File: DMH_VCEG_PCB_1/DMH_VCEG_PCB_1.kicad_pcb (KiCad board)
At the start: 2 copper layers, 148 x 175 mm, 229 parts, among them J1 TS_Jack_6.35mm_Sw, J10 TS_Jack_6.35mm_Sw, J100 IDC_02x08, J11 TS_Jack_6.35mm_Sw, J12 TS_Jack_6.35mm_Sw, J13 TS_Jack_6.35mm_Sw, J14 TS_Jack_6.35mm_Sw, J15 TS_Jack_6.35mm_Sw, J16 TS_Jack_6.35mm_Sw, J17 TS_Jack_6.35mm_Sw, J18 TS_Jack_6.35mm_Sw, J19 TS_Jack_6.35mm_Sw, J2 TS_Jack_6.35mm_Sw, J20 TS_Jack_6.35mm_Sw, J200 IDC_02x08, J21 Conn_01x10_PinHeader, J22 Conn_01x10_PinHeader, J23 Conn_01x10_PinHeader, J24 Conn_01x06_PinHeader, J25 Conn_01x10_PinHeader, J26 Conn_01x10_PinHeader, J27 Conn_01x10_PinHeader, J3 TS_Jack_6.35mm_Sw, J4 TS_Jack_6.35mm_Sw, J5 TS_Jack_6.35mm_Sw, J6 TS_Jack_6.35mm_Sw, J7 TS_Jack_6.35mm_Sw, J8 TS_Jack_6.35mm_Sw, J9 TS_Jack_6.35mm_Sw, Q1 BC558, Q17 BC558, Q18 BC558, Q19 BC548, Q2 BC558, Q20 BC548, Q21 MMBFJ113, Q22 MMBFJ113, Q3 BC548, Q4 BC548, Q5 MMBFJ113, Q6 MMBFJ113, U1 TL074, U11 TL074, U12 4001, U13 40106, U15 TL074, U16 4001, U17 TL074, U2 4001, U3 40106, U5 TL074, U6 4001, U7 TL074

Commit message: Started placement on PCB 2
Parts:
- C1, C2: footprint Capacitor_THT:CP_Radial_D4.0mm_P1.50mm -> Capacitor_THT:CP_Radial_D5.0mm_P2.00mm

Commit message: PCB 2 placement in progress
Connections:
- J22 pad 5: /CV Processing A/Att CV -> unconnected-(J22E-Pin_5-Pad5)
- J22 pad 6: /CV Processing A/Dec CV -> unconnected-(J22F-Pin_6-Pad6)
- J22 pad 7: /CV Processing A/Sus CV -> unconnected-(J22G-Pin_7-Pad7)
- J22 pad 8: /CV Processing A/Rel CV -> unconnected-(J22H-Pin_8-Pad8)
- J26 pad 5: /CV Processing B/Att CV -> unconnected-(J26E-Pin_5-Pad5)
- J26 pad 6: /CV Processing B/Dec CV -> unconnected-(J26F-Pin_6-Pad6)
- J26 pad 7: /CV Processing B/Sus CV -> unconnected-(J26G-Pin_7-Pad7)
- J26 pad 8: /CV Processing B/Rel CV -> unconnected-(J26H-Pin_8-Pad8)
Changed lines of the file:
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@@
 	(net 185 "Net-(D13-K)")
 	(net 186 "Net-(D13-A)")
+	(net 187 "unconnected-(J22H-Pin_8-Pad8)")
+	(net 188 "unconnected-(J22F-Pin_6-Pad6)")
+	(net 189 "unconnected-(J22G-Pin_7-Pad7)")
+	(net 190 "unconnected-(J22E-Pin_5-Pad5)")
+	(net 191 "unconnected-(J26E-Pin_5-Pad5)")
+	(net 192 "unconnected-(J26H-Pin_8-Pad8)")
+	(net 193 "unconnected-(J26F-Pin_6-Pad6)")
+	(net 194 "unconnected-(J26G-Pin_7-Pad7)")
 	(footprint "Resistor_THT:R_Axial_DIN0207_L6.3mm_D2.5mm_P7.62mm_Horizontal"
 		(layer "F.Cu")
@@
 			(layers "*.Cu" "*.Mask")
 			(remove_unused_layers no)
-			(net 122 "/CV Processing B/Att CV")
+			(net 191 "unconnected-(J26E-Pin_5-Pad5)")
 			(pinfunction "Pin_5")
-			(pintype "passive")
+			(pintype "passive+no_connect")
 		)
 		(pad "6" thru_hole circle
@@
 			(layers "*.Cu" "*.Mask")
 			(remove_unused_layers no)
-			(net 127 "/CV Processing B/Dec CV")
+			(net 193 "unconnected-(J26F-Pin_6-Pad6)")
 			(pinfunction "Pin_6")
-			(pintype "passive")
+			(pintype "passive+no_connect")
 		)
 		(pad "7" thru_hole circle
@@
 			(layers "*.Cu" "*.Mask")
 			(remove_unused_layers no)
-			(net 133 "/CV Processing B/Sus CV")
+			(net 194 "unconnected-(J26G-Pin_7-Pad7)")
 			(pinfunction "Pin_7")
-			(pintype "passive")
+			(pintype "passive+no_connect")
 		)
 		(pad "8" thru_hole circle
@@
 			(layers "*.Cu" "*.Mask")
 			(remove_unused_layers no)
-			(net 126 "/CV Processing B/Rel CV")
+			(net 192 "unconnected-(J26H-Pin_8-Pad8)")
 			(pinfunction "Pin_8")
-			(pintype "passive")
+			(pintype "passive+no_connect")
 		)
 		(pad "9" thru_hole circle
@@
 			(layers "*.Cu" "*.Mask")
 			(remove_unused_layers no)
-			(net 91 "/CV Processing A/Att CV")
+			(net 190 "unconnected-(J22E-Pin_5-Pad5)")
 			(pinfunction "Pin_5")
-			(pintype "passive")
+			(pintype "passive+no_connect")
 		)
 		(pad "6" thru_hole circle
@@
 			(layers "*.Cu" "*.Mask")
 			(remove_unused_layers no)
-			(net 92 "/CV Processing A/Dec CV")
+			(net 188 "unconnected-(J22F-Pin_6-Pad6)")
 			(pinfunction "Pin_6")
-			(pintype "passive")
+			(pintype "passive+no_connect")
 		)
 		(pad "7" thru_hole circle
@@
 			(layers "*.Cu" "*.Mask")
 			(remove_unused_layers no)
-			(net 98 "/CV Processing A/Sus CV")
+			(net 189 "unconnected-(J22G-Pin_7-Pad7)")
 			(pinfunction "Pin_7")
-			(pintype "passive")
+			(pintype "passive+no_connect")
 		)
 		(pad "8" thru_hole circle
@@
 			(layers "*.Cu" "*.Mask")
 			(remove_unused_layers no)
-			(net 99 "/CV Processing A/Rel CV")
+			(net 187 "unconnected-(J22H-Pin_8-Pad8)")
 			(pinfunction "Pin_8")
-			(pintype "passive")
+			(pintype "passive+no_connect")
 		)
 		(pad "9" thru_hole circle

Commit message: PCB 2 routing in progress
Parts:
- removed R108, R115, R116: 100k, Resistor_THT:R_Axial_DIN0207_L6.3mm_D2.5mm_P7.62mm_Horizontal
- added R195: 100R, Resistor_THT:R_Axial_DIN0207_L6.3mm_D2.5mm_P7.62mm_Horizontal, F.Cu at (197.4, 139.2)
- added R196: 47k, Resistor_THT:R_Axial_DIN0207_L6.3mm_D2.5mm_P7.62mm_Horizontal, F.Cu at (197.4, 143.2)
- added R197: 68k, Resistor_THT:R_Axial_DIN0207_L6.3mm_D2.5mm_P7.62mm_Horizontal, F.Cu at (210.1, 139.2)
- added R198: 100k, Resistor_THT:R_Axial_DIN0207_L6.3mm_D2.5mm_P7.62mm_Horizontal, F.Cu at (210.1, 143.2)
- added R199: 100R, Resistor_THT:R_Axial_DIN0207_L6.3mm_D2.5mm_P7.62mm_Horizontal, F.Cu at (210.1, 149.2)
- Q21, Q22, Q5, Q6: value MMBFJ113 -> BS170; footprint Package_TO_SOT_THT:TO-92L_Inline -> Package_TO_SOT_THT:TO-92_Inline
- R129, R32: value 100k -> 51k
- R131, R19, R34: value 100k -> 47k
- R18: value 100k -> 68k
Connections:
- C46 pad 1: Net-(D13-K) -> /Core Circuit A/ProcGate
- C48 pad 2: /Core Circuit A/ProcGate -> Net-(D5-A)
- C62 pad 1: Net-(D22-K) -> /Core Circuit B/ProcGate
- C64 pad 2: /Core Circuit B/ProcGate -> Net-(D24-A)
- D22 pad 1: Net-(D22-K) -> /Core Circuit B/ProcGate
- D24 pad 1: Net-(D22-K) -> /Core Circuit B/ProcGate
- D24 pad 2: /Core Circuit B/ProcGate -> Net-(D24-A)
- D3 pad 1: Net-(D13-K) -> /Core Circuit A/ProcGate
- D32 pad 1: Net-(D22-K) -> Net-(D32-K)
- D5 pad 1: Net-(D13-K) -> /Core Circuit A/ProcGate
- D5 pad 2: /Core Circuit A/ProcGate -> Net-(D5-A)
- J21 pad 3: /Core Circuit A/Sus State -> /Core Circuit A/Sus_State
- J22 pad 2: /Core Circuit A/Sus State -> /Core Circuit A/Inv Sus State
- J22 pad 5: unconnected-(J22E-Pin_5-Pad5) -> /CV Processing A/Att CV
- J22 pad 6: unconnected-(J22F-Pin_6-Pad6) -> /CV Processing A/Dec CV
- J22 pad 7: unconnected-(J22G-Pin_7-Pad7) -> /CV Processing A/Sus CV
- J22 pad 8: unconnected-(J22H-Pin_8-Pad8) -> /CV Processing A/Rel CV
- J23 pad 10: /CV Processing A/Rel CV -> unconnected-(J23J-Pin_10-Pad10)
- J23 pad 3: /CV Processing A/Att CV -> unconnected-(J23C-Pin_3-Pad3)
- J23 pad 6: /CV Processing A/Dec CV -> unconnected-(J23F-Pin_6-Pad6)
- J23 pad 7: /CV Processing A/Sus CV -> unconnected-(J23G-Pin_7-Pad7)
- J24 pad 2: Net-(D13-A) -> /Core Circuit A/ProcGate
- J24 pad 3: Net-(J24C-Pin_3) -> Net-(D13-K)
- J24 pad 4: Net-(J24D-Pin_4) -> Net-(D32-K)
- J24 pad 5: Net-(D32-A) -> /Core Circuit B/ProcGate
- J25 pad 3: /Core Circuit B/Sus State -> /Core Circuit B/Sus_State
- J26 pad 2: /Core Circuit B/Sus State -> /Core Circuit B/Inv Sus State
- J26 pad 5: unconnected-(J26E-Pin_5-Pad5) -> /CV Processing B/Att CV
- J26 pad 6: unconnected-(J26F-Pin_6-Pad6) -> /CV Processing B/Dec CV
- J26 pad 7: unconnected-(J26G-Pin_7-Pad7) -> /CV Processing B/Sus CV
- J26 pad 8: unconnected-(J26H-Pin_8-Pad8) -> /CV Processing B/Rel CV
- J27 pad 10: /CV Processing B/Rel CV -> unconnected-(J27J-Pin_10-Pad10)
- J27 pad 3: /CV Processing B/Att CV -> unconnected-(J27C-Pin_3-Pad3)
- J27 pad 6: /CV Processing B/Dec CV -> unconnected-(J27F-Pin_6-Pad6)
- J27 pad 7: /CV Processing B/Sus CV -> unconnected-(J27G-Pin_7-Pad7)
- Q21 pad 1: Net-(Q18-C) -> Net-(J25F-Pin_6)
- Q21 pad 2: Net-(J25F-Pin_6) -> /Core Circuit B/ProcGate
- Q21 pad 3: Net-(Q21-G) -> Net-(Q18-C)
- Q22 pad 1: Net-(Q20-C) -> Net-(J25F-Pin_6)
- Q22 pad 2: Net-(J25F-Pin_6) -> /Core Circuit B/InvGate
- Q22 pad 3: Net-(Q22-G) -> Net-(Q20-C)
- Q5 pad 1: Net-(Q2-C) -> Net-(J21F-Pin_6)
- Q5 pad 2: Net-(J21F-Pin_6) -> /Core Circuit A/ProcGate
- Q5 pad 3: Net-(Q5-G) -> Net-(Q2-C)
- Q6 pad 1: Net-(Q4-C) -> Net-(J21F-Pin_6)
- Q6 pad 2: Net-(J21F-Pin_6) -> /Core Circuit A/InvGate
- Q6 pad 3: Net-(Q6-G) -> Net-(Q4-C)
- R11 pad 1: Net-(Q5-G) -> Net-(R11-Pad1)
- R11 pad 2: /Core Circuit A/ProcGate -> GND
- R120 pad 1: /Core Circuit B/ProcGate -> Net-(D24-A)
- R121 pad 2: Net-(D22-K) -> /Core Circuit B/ProcGate
- R131 pad 1: Net-(J24D-Pin_4) -> Net-(D32-A)
- R134 pad 1: Net-(U15A-+) -> Net-(U15A--)
- R138 pad 1: -12V -> Net-(U15A-+)
- R138 pad 2: Net-(U15A--) -> Net-(D34-A)
- R141 pad 1: Net-(U15A--) -> Net-(U15A-+)
- R18 pad 1: -12V -> +12V
- R18 pad 2: Net-(Q6-G) -> Net-(R11-Pad1)
- R19 pad 1: Net-(Q6-G) -> GND
- R19 pad 2: /Core Circuit A/InvGate -> Net-(U15C--)
- R23 pad 1: /Core Circuit A/ProcGate -> Net-(D5-A)
- R24 pad 2: Net-(D13-K) -> /Core Circuit A/ProcGate
- R34 pad 1: Net-(J24C-Pin_3) -> Net-(D13-A)
- R37 pad 1: Net-(U5A-+) -> Net-(U5A--)
- R41 pad 1: -12V -> Net-(D15-A)
- R41 pad 2: Net-(U5A--) -> Net-(U5A-+)
- R44 pad 1: Net-(U5A--) -> GND
- R44 pad 2: GND -> Net-(U5A-+)
- U1 pad 1: /Core Circuit A/ProcGate -> Net-(D5-A)
- U1 pad 14: Net-(J24C-Pin_3) -> Net-(D13-A)
- U1 pad 8: Net-(U5A-+) -> Net-(U5A--)
- U11 pad 1: /Core Circuit B/ProcGate -> Net-(D24-A)
- U11 pad 14: Net-(J24D-Pin_4) -> Net-(D32-A)
- U11 pad 8: Net-(U15A-+) -> Net-(U15A--)
- U13 pad 1: Net-(D22-K) -> /Core Circuit B/ProcGate
- U13 pad 4: Net-(U13-Pad4) -> Net-(D35-A)
- U13 pad 8: unconnected-(U13-Pad8) -> Net-(U13-Pad8)
- U13 pad 9: GND -> Net-(C71-Pad2)
- U15 pad 9: /CV Processing B/Max Level -> Net-(U15C--)
- U16 pad 10: Net-(D35-A) -> Net-(U16-Pad10)
- U16 pad 13: /Core Circuit B/Sus State -> /Core Circuit B/Sus_State
- U16 pad 2: Net-(U16-Pad2) -> /Core Circuit B/Inv Sus State
- U16 pad 3: /Core Circuit B/Sus State -> /Core Circuit B/Sus_State
- U16 pad 4: Net-(U16-Pad2) -> /Core Circuit B/Inv Sus State
- U16 pad 5: /Core Circuit B/Sus State -> /Core Circuit B/Sus_State
- U16 pad 6: Net-(C71-Pad2) -> Net-(U16-Pad10)
- U16 pad 9: Net-(U13-Pad4) -> Net-(U13-Pad8)
- U3 pad 1: Net-(D13-K) -> /Core Circuit A/ProcGate
- U3 pad 4: Net-(U3-Pad4) -> Net-(D16-A)
- U3 pad 8: unconnected-(U3-Pad8) -> Net-(U3-Pad8)
- U3 pad 9: GND -> Net-(C55-Pad2)
- U5 pad 9: /CV Processing A/Max Level -> Net-(U5C--)
- U6 pad 10: Net-(D16-A) -> Net-(U6-Pad10)
- U6 pad 13: /Core Circuit A/Sus State -> /Core Circuit A/Sus_State
- U6 pad 2: Net-(U6-Pad2) -> /Core Circuit A/Inv Sus State
- U6 pad 3: /Core Circuit A/Sus State -> /Core Circuit A/Sus_State
- U6 pad 4: Net-(U6-Pad2) -> /Core Circuit A/Inv Sus State
- U6 pad 5: /Core Circuit A/Sus State -> /Core Circuit A/Sus_State
- U6 pad 6: Net-(C55-Pad2) -> Net-(U6-Pad10)
- U6 pad 9: Net-(U3-Pad4) -> Net-(U3-Pad8)

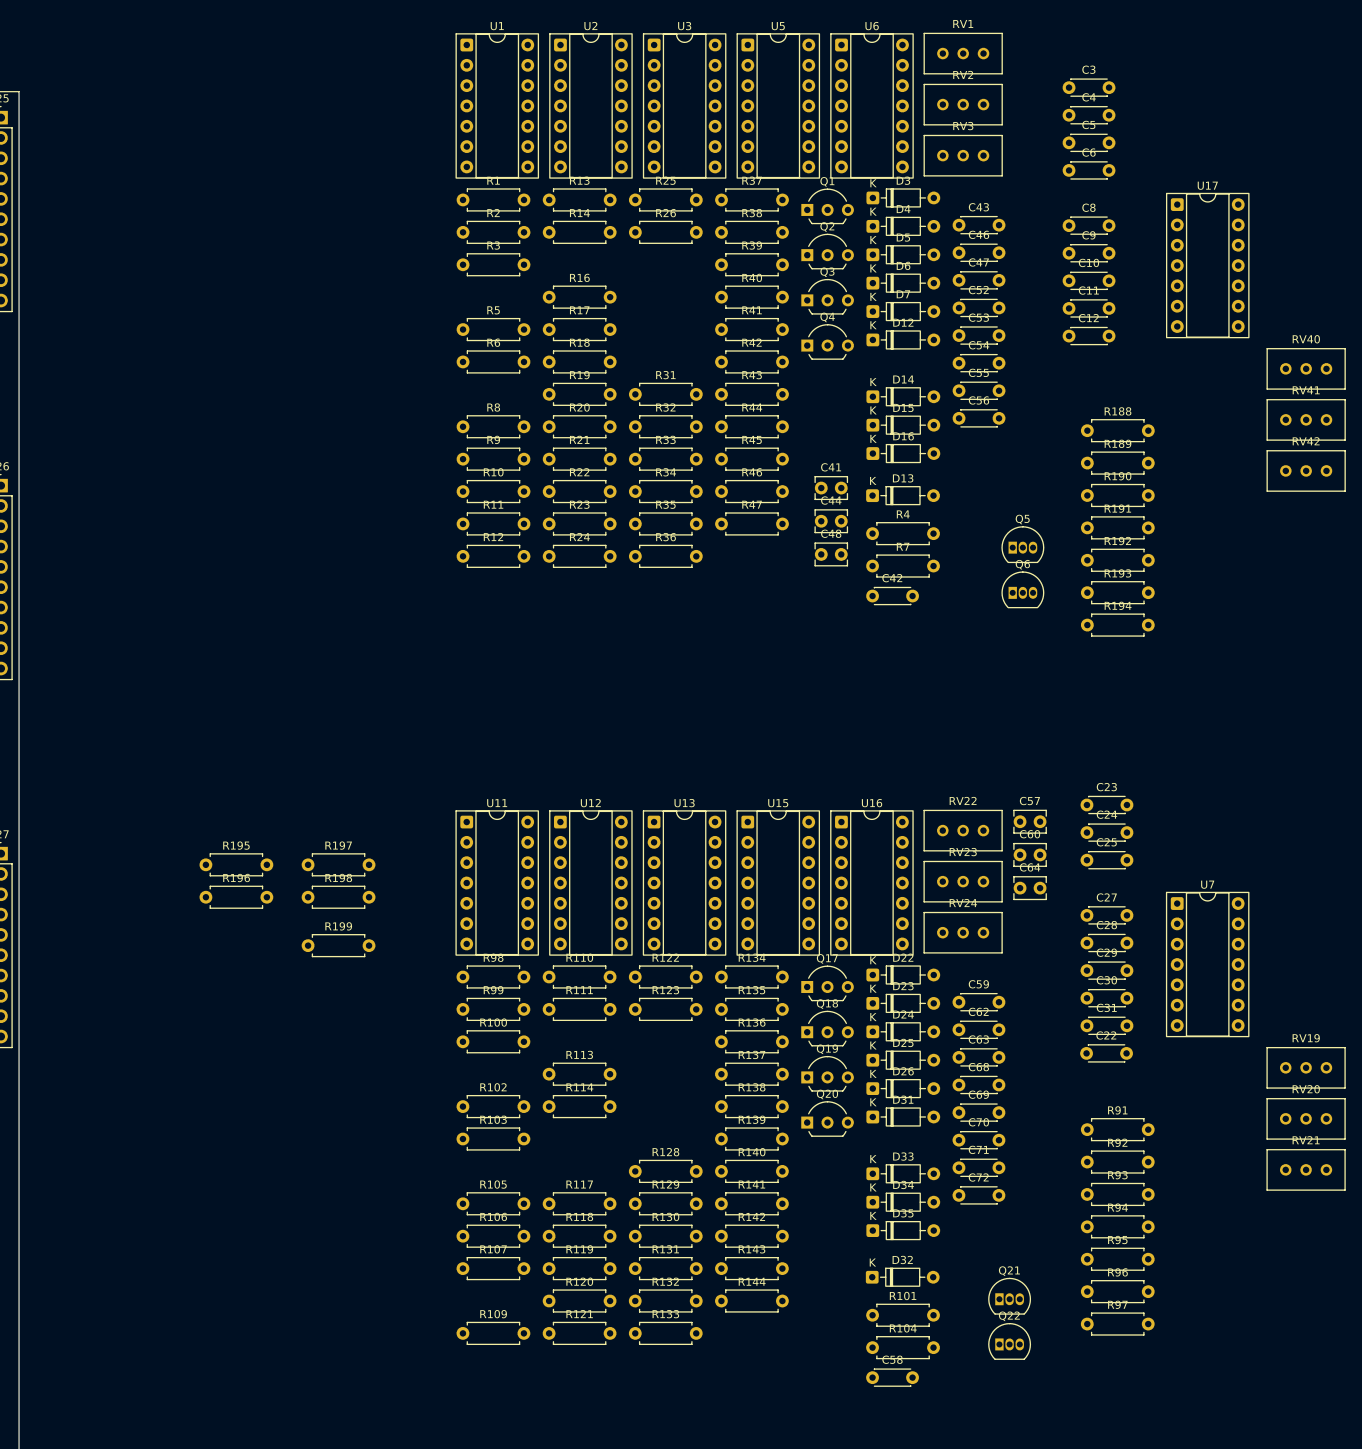
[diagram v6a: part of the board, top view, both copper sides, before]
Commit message: Synced PCB 1 and 2
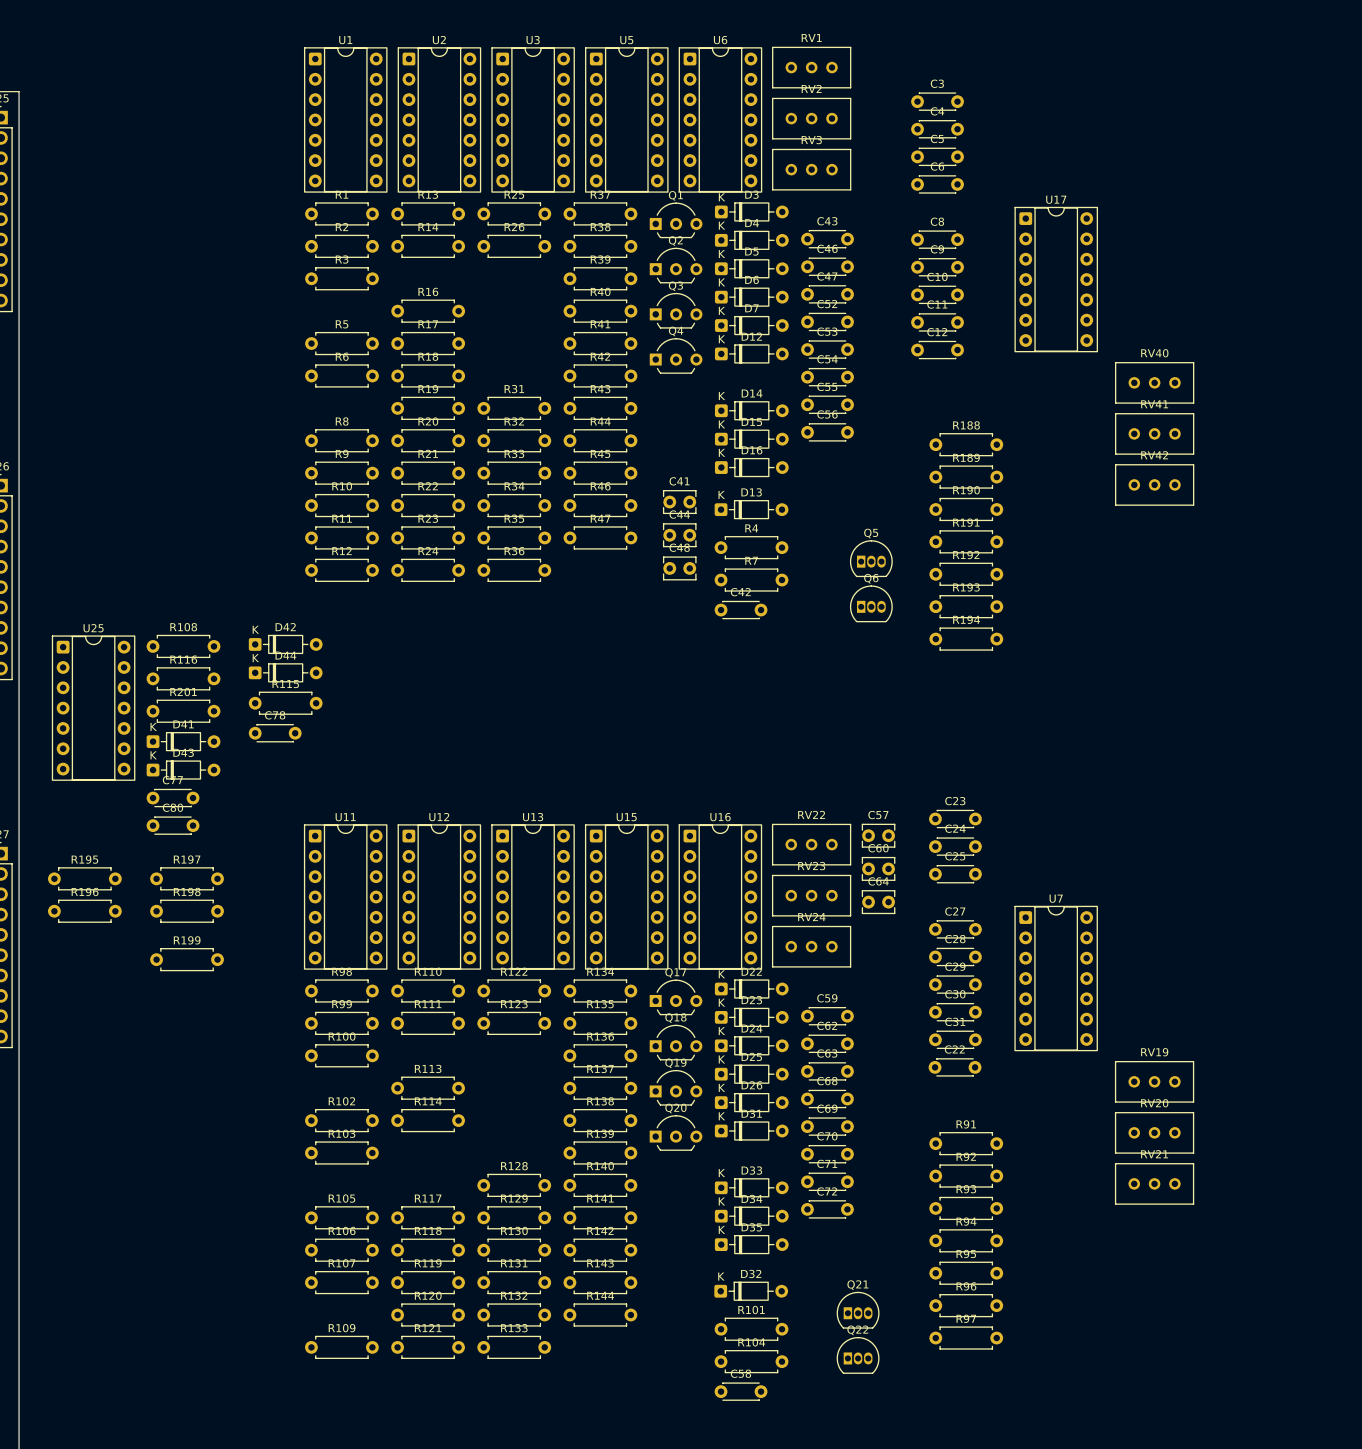
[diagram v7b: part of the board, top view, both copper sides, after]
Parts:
- added C77: 10nF, Capacitor_THT:C_Disc_D4.3mm_W1.9mm_P5.00mm, F.Cu at (190.8, 130.8)
- added C78: 10nF, Capacitor_THT:C_Disc_D4.3mm_W1.9mm_P5.00mm, F.Cu at (203.5, 122.7)
- added C80: 10nF, Capacitor_THT:C_Disc_D4.3mm_W1.9mm_P5.00mm, F.Cu at (190.8, 134.2)
- added D41: 1N4148, Diode_THT:D_DO-35_SOD27_P7.62mm_Horizontal, F.Cu at (190.8, 123.8)
- added D42: 1N4148, Diode_THT:D_DO-35_SOD27_P7.62mm_Horizontal, F.Cu at (203.5, 111.6)
- added D43: 1N4148, Diode_THT:D_DO-35_SOD27_P7.62mm_Horizontal, F.Cu at (190.8, 127.3)
- added D44: 1N4148, Diode_THT:D_DO-35_SOD27_P7.62mm_Horizontal, F.Cu at (203.5, 115.2)
- added R108: 10k, Resistor_THT:R_Axial_DIN0207_L6.3mm_D2.5mm_P7.62mm_Horizontal, F.Cu at (190.8, 111.8)
- added R115: 10k, Resistor_THT:R_Axial_DIN0207_L6.3mm_D2.5mm_P7.62mm_Horizontal, F.Cu at (203.5, 119.0)
- added R116: 10k, Resistor_THT:R_Axial_DIN0207_L6.3mm_D2.5mm_P7.62mm_Horizontal, F.Cu at (190.8, 115.9)
- added R201: 100k, Resistor_THT:R_Axial_DIN0207_L6.3mm_D2.5mm_P7.62mm_Horizontal, F.Cu at (190.8, 120.0)
- added U25: 4001, Package_DIP:DIP-14_W7.62mm_Socket, F.Cu at (179.5, 111.9)
- C72: value 10nF -> 100nF
- R129: value 51k -> 100k
- R130, R33: value 100k -> 100R
- R141, R44: value 100R -> 220R
- R32: value 51k -> 10k
- moved D22 19.0 mm to (261.8, 154.7)
- moved D23 19.0 mm to (261.8, 158.2)
- moved D24 19.0 mm to (261.8, 161.8)
- moved D25 19.0 mm to (261.8, 165.3)
- moved D26 19.0 mm to (261.8, 168.9)
- moved D31 19.0 mm to (261.8, 172.4)
- moved D33 19.0 mm to (261.8, 179.5)
- moved D34 19.0 mm to (261.8, 183.1)
- moved D35 19.0 mm to (261.8, 186.6)
- moved R195 19.0 mm to (178.4, 140.9)
- moved R196 19.0 mm to (178.4, 144.9)
- moved U5 19.0 mm to (246.2, 38.4)
- moved C10 19.0 mm to (286.3, 67.9)
- moved C11 19.0 mm to (286.3, 71.3)
- moved C12 19.0 mm to (286.3, 74.8)
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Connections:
- net Net-(C52-Pad2) renamed /Core Circuit A/Sus_Reset
- net Net-(C68-Pad2) renamed /Core Circuit B/Sus_Reset
- C56 pad 1: GND -> Net-(C56-Pad1)
- C56 pad 2: Net-(C56-Pad2) -> Net-(D44-K)
- C72 pad 1: GND -> +12V
- C72 pad 2: Net-(C72-Pad2) -> GND
- J24 pad 2: /Core Circuit A/ProcGate -> Net-(J24B-Pin_2)
- J24 pad 3: Net-(D13-K) -> /Core Circuit A/ProcGate
- J24 pad 4: Net-(D32-K) -> Net-(J24D-Pin_4)
- R129 pad 1: Net-(U11D-+) -> Net-(C56-Pad1)
- R129 pad 2: +12V -> GND
- R131 pad 1: Net-(D32-A) -> +12V
- R138 pad 2: Net-(D34-A) -> -12V
- R140 pad 1: Net-(D34-K) -> GND
- R140 pad 2: Net-(C72-Pad2) -> Net-(D44-K)
- R17 pad 1: GND -> Net-(U1A--)
- R17 pad 2: Net-(U1A--) -> GND
- R32 pad 1: Net-(U1D-+) -> GND
- R32 pad 2: +12V -> Net-(D13-K)
- R34 pad 1: Net-(D13-A) -> +12V
- R41 pad 1: Net-(D15-A) -> -12V
- R43 pad 1: Net-(D15-K) -> GND
- R43 pad 2: Net-(C56-Pad2) -> Net-(D32-K)
- U13 pad 3: Net-(C72-Pad2) -> Net-(D34-K)
- U3 pad 3: Net-(C56-Pad2) -> Net-(D15-K)
